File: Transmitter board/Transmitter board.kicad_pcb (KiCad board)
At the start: 2 copper layers, 26.4 x 37 mm, 25 parts, among them J3 Conn_01x02_Male, J4 Conn_01x03_Male, J5 Conn_01x04_Male, J6 Conn_01x03_Male, J7 Conn_01x05_Male, J8 Conn_01x02_Male, SW1 SW_Push, U1 RFM69HCW, U2 LPC824_HVQFN33, U3 SWD_10-pin-1.27_Conn_2x5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

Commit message: inished Minimized Disc Transmitter
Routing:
- net GND: track 82.1 -> 81.2 mm
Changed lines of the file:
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@@
     (thickness 1.6)
     (drawings 42)
-    (tracks 369)
+    (tracks 368)
     (zones 0)
     (modules 25)
@@
   (segment (start 90.200001 54.899999) (end 90.6 54.5) (width 0.25) (layer B.Cu) (net 1))
   (segment (start 88.35 56.75) (end 90.200001 54.899999) (width 0.25) (layer B.Cu) (net 1))
-  (segment (start 88.35 57.65) (end 88.35 56.75) (width 0.25) (layer B.Cu) (net 1))
   (segment (start 90.47652 54.62348) (end 90.6 54.5) (width 0.25) (layer F.Cu) (net 1))
   (segment (start 89.477651 54.62348) (end 90.47652 54.62348) (width 0.25) (layer F.Cu) (net 1))
@@
   (segment (start 89.6 77.9) (end 89 77.3) (width 0.25) (layer B.Cu) (net 1))
   (via (at 69.7 80.4) (size 0.8) (drill 0.4) (layers F.Cu B.Cu) (net 1))
+  (segment (start 93.2 64.05) (end 92.776996 64.05) (width 0.25) (layer B.Cu) (net 2))
   (segment (start 83.97 72.83) (end 82.7 72.83) (width 0.25) (layer B.Cu) (net 2))
+  (segment (start 87.9 69.45) (end 87.35 69.45) (width 0.25) (layer B.Cu) (net 2))
   (segment (start 87.35 69.45) (end 83.97 72.83) (width 0.25) (layer B.Cu) (net 2))
-  (segment (start 93.2 64.05) (end 92.776996 64.05) (width 0.25) (layer B.Cu) (net 2))
-  (segment (start 87.9 69.45) (end 87.35 69.45) (width 0.25) (layer B.Cu) (net 2))
+  (segment (start 92.75 64.05) (end 90.841596 65.958404) (width 0.25) (layer B.Cu) (net 2))
+  (segment (start 93.2 64.05) (end 92.75 64.05) (width 0.25) (layer B.Cu) (net 2))
+  (segment (start 90.841596 65.958404) (end 90.841596 66.458404) (width 0.25) (layer B.Cu) (net 2))
+  (segment (start 90.841596 66.458404) (end 89.836395 67.463605) (width 0.25) (layer B.Cu) (net 2))
+  (segment (start 89.836395 67.463605) (end 89.836395 67.513605) (width 0.25) (layer B.Cu) (net 2))
   (segment (start 89.836395 67.513605) (end 87.9 69.45) (width 0.25) (layer B.Cu) (net 2))
-  (segment (start 89.836395 67.513605) (end 89.836395 67.463605) (width 0.25) (layer B.Cu) (net 2))
-  (segment (start 90.841596 66.458404) (end 90.841596 65.958404) (width 0.25) (layer B.Cu) (net 2))
-  (segment (start 89.836395 67.463605) (end 90.841596 66.458404) (width 0.25) (layer B.Cu) (net 2))
-  (segment (start 92.75 64.05) (end 93.2 64.05) (width 0.25) (layer B.Cu) (net 2))
-  (segment (start 90.841596 65.958404) (end 92.75 64.05) (width 0.25) (layer B.Cu) (net 2))
   (via (at 84.8 78.3) (size 0.8) (drill 0.4) (layers F.Cu B.Cu) (net 3))
   (segment (start 87.7 78.75) (end 85.25 78.75) (width 0.25) (layer F.Cu) (net 3))

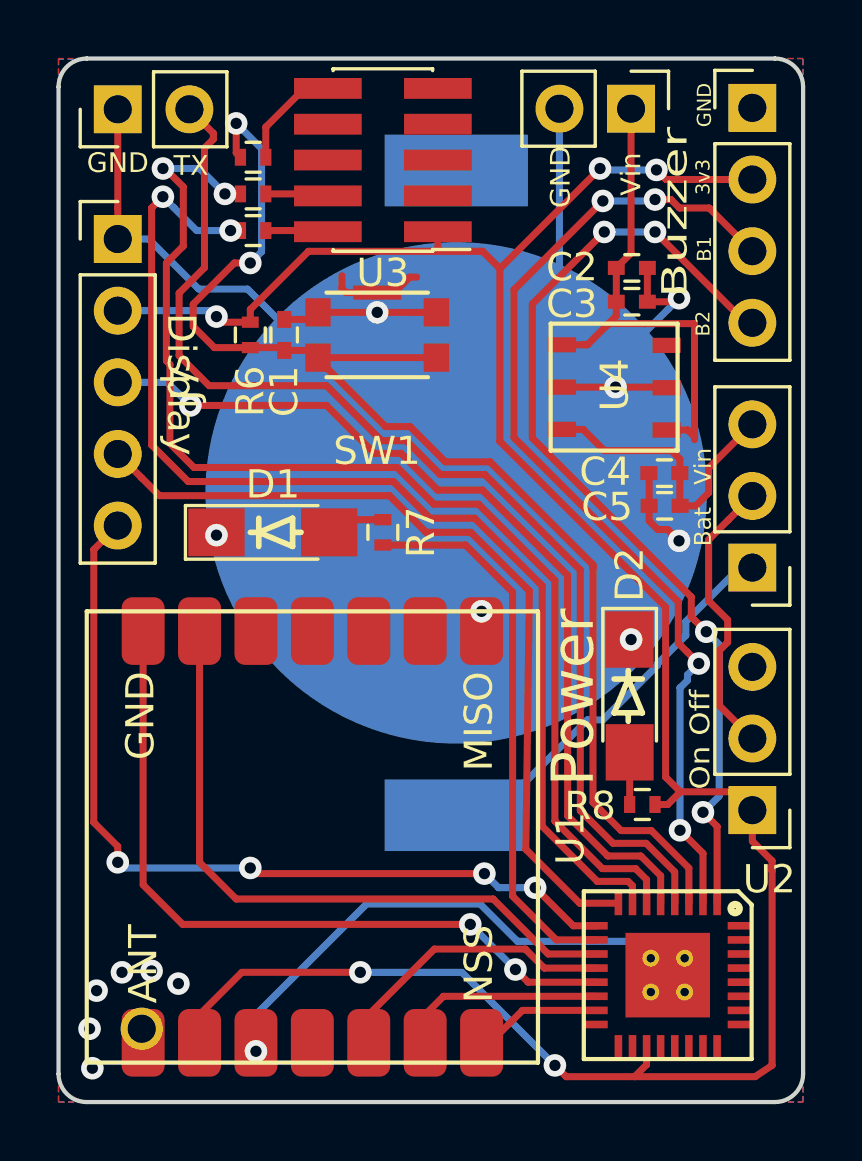
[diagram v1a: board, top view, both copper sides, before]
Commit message: Fixed pads on RFM footprint
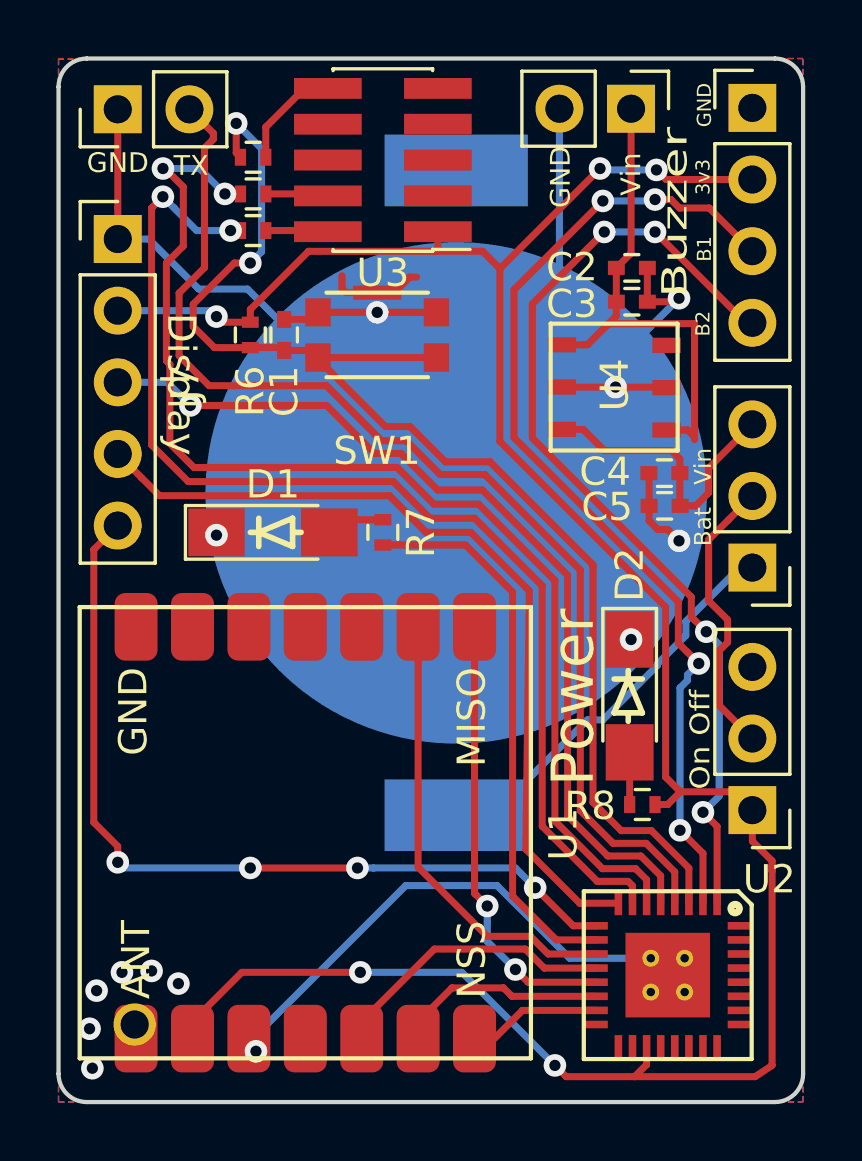
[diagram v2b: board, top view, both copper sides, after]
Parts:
- R8: value 750ohm -> 330ohm
- U1: footprint my_foot_prints:RFM96C -> my_foot_prints:RFM96HCW
- moved U1 0.29 mm to (77.3, 73.5)
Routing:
- net MISO: track 27.2 -> 15.9 mm
- net DIO0: track 24.3 -> 16.2 mm
- net GND: track 81.2 -> 81.3 mm, vias 14 -> 13

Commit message: V2
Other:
- board text added: "Version 2"
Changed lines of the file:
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@@
   (general
     (thickness 1.6)
-    (drawings 42)
+    (drawings 43)
     (tracks 371)
     (zones 0)
@@
       (net 52 "Net-(U1-Pad1)"))
   )
+  (gr_text "Version 2" (at 82.25 80.55 180) (layer B.SilkS)
+    (effects (font (size 1 1) (thickness 0.25)) (justify mirror))
+  )
   (gr_arc (start 94 47) (end 95 47) (angle -90) (layer Edge.Cuts) (width 0.15))
